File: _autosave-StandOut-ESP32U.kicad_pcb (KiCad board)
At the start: 4 copper layers, 101.9 x 58.2 mm, 20 parts, among them J1 UART_2, J10 Common Pins, J11 GPIO, J12 GPIO, J13 Conn_01x18_Male, J16 Conn_01x18_Male, J2 GPIO, J3 Common Pins, J4 UART_0, J5 GPIO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

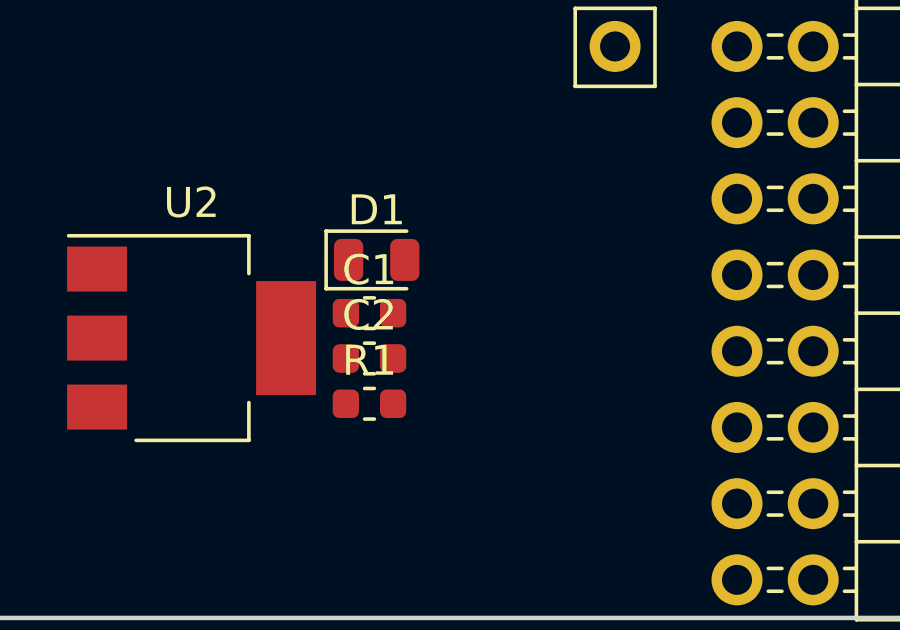
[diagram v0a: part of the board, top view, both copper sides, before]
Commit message: Working on Schematic - Micro-USB & UART
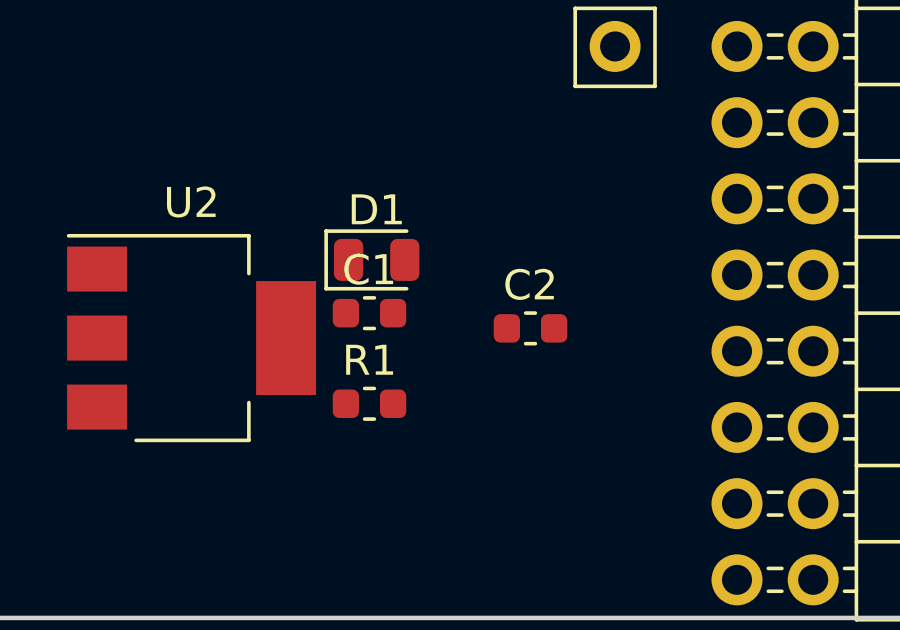
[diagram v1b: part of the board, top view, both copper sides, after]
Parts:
- moved C2 5.46 mm to (118.6, 137.7)
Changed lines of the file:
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@@
   )
   (module Capacitor_SMD:C_0603_1608Metric (layer F.Cu)
-    (at 113.225001 138.671001)
+    (at 118.5925 137.668)
     (descr "Capacitor SMD 0603 (1608 Metric), square (rectangular) end terminal, IPC_7351 nominal, (Body size source: http://www.tortai-tech.com/upload/download/2011102023233369053.pdf), generated with kicad-footprint-generator")
     (tags capacitor)
